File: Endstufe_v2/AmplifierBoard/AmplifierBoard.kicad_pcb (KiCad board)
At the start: 2 copper layers, 125 x 90 mm, 116 parts, among them J1 Conn_01x01_Pin, J10 Conn_02x06_Top_Bottom, J11 B6B-XH-2(LF)(SN), J12 B6B-XH-2(LF)(SN), J13 Conn_01x02_Pin, J14 Conn_01x02_Pin, J15 Conn_01x02_Pin, J16 Conn_01x04, J17 Conn_01x02_Pin, J2 Conn_01x01_Pin, J3 banana connector, J4 banana connector, J5 banana connector, J6 banana connector, J7 banana connector, J8 banana connector, J9 ST-0322D00-071-1A2H, U1 TPA3126D2DADR, U2 TPA3126D2DADR, U3 NVTFWS014P04M8LTAG, U4 1SMA5927A

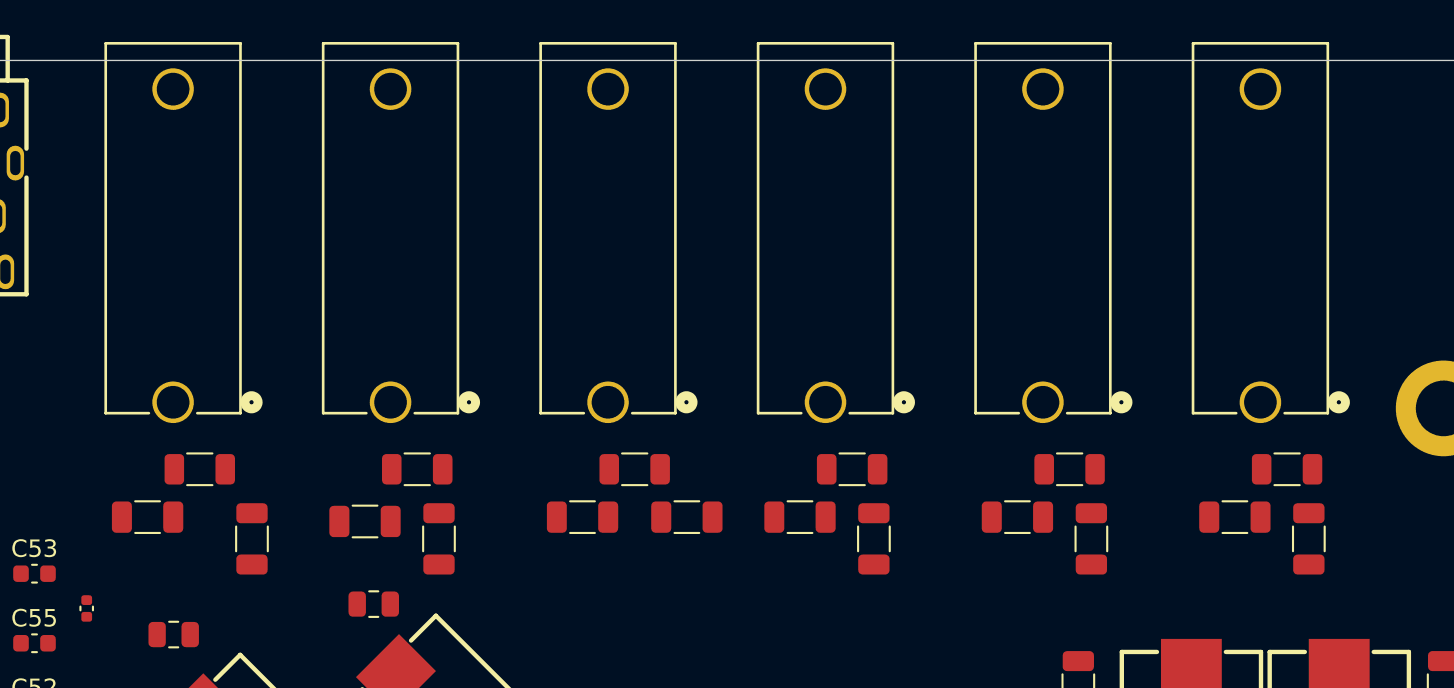
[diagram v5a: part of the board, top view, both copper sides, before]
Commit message: Finalize layout and check DRC
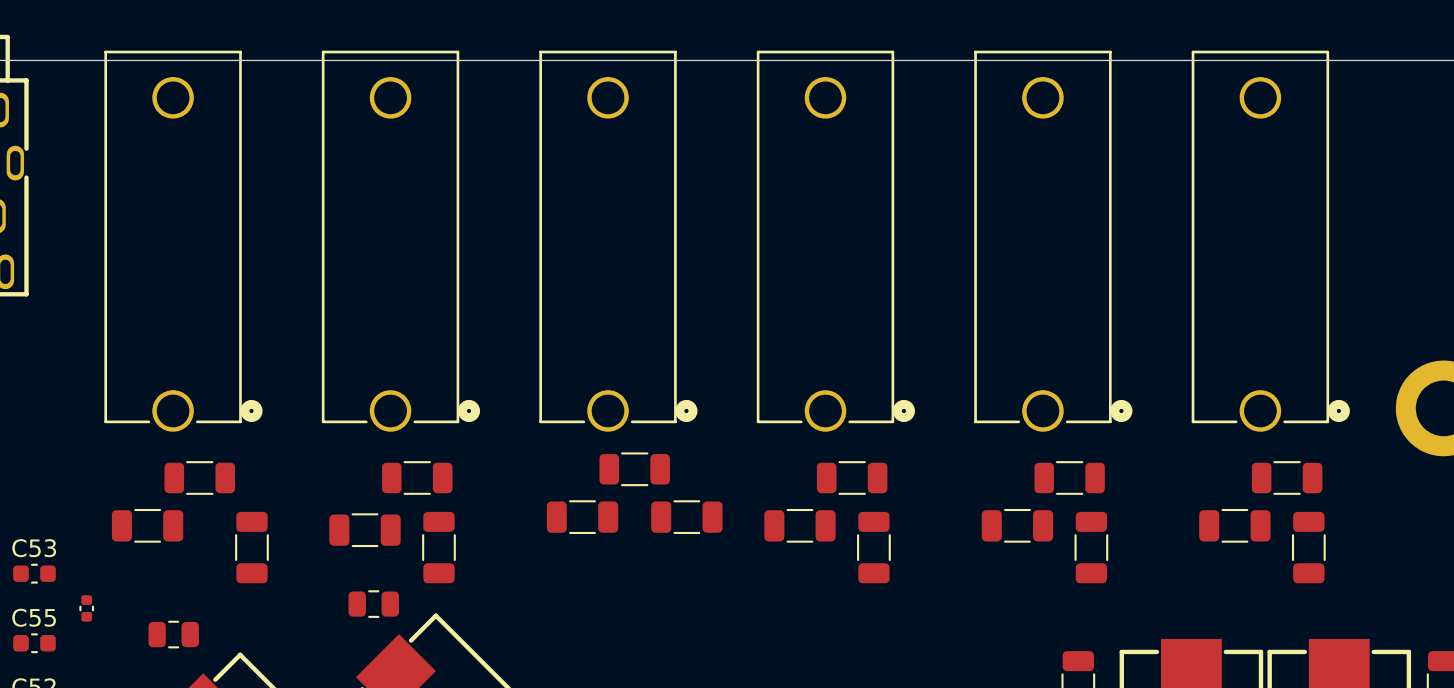
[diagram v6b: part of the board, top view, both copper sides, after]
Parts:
- moved C41 0.50 mm to (193.0, 76.8)
- moved C42 0.50 mm to (205.5, 76.8)
- moved C43 0.50 mm to (218.0, 76.8)
- moved C44 0.50 mm to (155.5, 76.8)
- moved C45 0.50 mm to (168.0, 77.0)
- moved C47 0.50 mm to (197.2, 78.0)
- moved C48 0.50 mm to (209.8, 78.0)
- moved C49 0.50 mm to (222.2, 78.0)
- moved C50 0.50 mm to (161.5, 78.0)
- moved C51 0.50 mm to (172.2, 78.0)
- moved J3 0.50 mm to (182.0, 70.1)
- moved J4 0.50 mm to (194.5, 70.1)
- moved J5 0.50 mm to (207.0, 70.1)
- moved J6 0.50 mm to (219.5, 70.1)
- moved J7 0.50 mm to (157.0, 70.1)
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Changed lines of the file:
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@@
 	(footprint "Endstufe:R_1206_3216Metric"
 		(layer "F.Cu")
-		(at 221 73.5 180)
+		(at 221 74 180)
 		(descr "Resistor SMD 1206 (3216 Metric), square (rectangular) end terminal, IPC_7351 nominal, (Body size source: IPC-SM-782 page 72, https://www.pcb-3d.com/wordpress/wp-content/uploads/ipc-sm-782a_amendment_1_and_2.pdf), generated with kicad-footprint-generator")
 		(tags "resistor")
@@
 	(footprint "Endstufe:C_1206_3216Metric"
 		(layer "F.Cu")
-		(at 155.5 76.25 180)
+		(at 155.5 76.75 180)
 		(descr "Capacitor SMD 1206 (3216 Metric), square (rectangular) end terminal, IPC_7351 nominal, (Body size source: IPC-SM-782 page 76, https://www.pcb-3d.com/wordpress/wp-content/uploads/ipc-sm-782a_amendment_1_and_2.pdf), generated with kicad-footprint-generator")
 		(tags "capacitor")
@@
 	(footprint "Endstufe:C_1206_3216Metric"
 		(layer "F.Cu")
-		(at 172.25 77.5 90)
+		(at 172.25 78 90)
 		(descr "Capacitor SMD 1206 (3216 Metric), square (rectangular) end terminal, IPC_7351 nominal, (Body size source: IPC-SM-782 page 76, https://www.pcb-3d.com/wordpress/wp-content/uploads/ipc-sm-782a_amendment_1_and_2.pdf), generated with kicad-footprint-generator")
 		(tags "capacitor")
@@
 		(tags "capacitor")
 		(property "Reference" "C52"
-			(at 0 -1.43 360)
+			(at 0 -1.43 0)
 			(layer "F.SilkS")
 			(effects
@@
 		)
 		(property "Value" "180nF"
-			(at 0 1.43 360)
+			(at 0 1.43 0)
 			(layer "F.Fab")
 			(effects
@@
 		)
 		(fp_text user "${REFERENCE}"
-			(at 0 0 360)
+			(at 0 0 0)
 			(layer "F.Fab")
 			(effects
@@
 	(footprint "Endstufe:CONN_973582100_HRS"
 		(layer "F.Cu")
-		(at 206.9666 69.648001 180)
+		(at 206.9666 70.148001 180)
 		(tags "973582100 ")
 		(property "Reference" "J5"
@@
 	(footprint "Endstufe:R_1206_3216Metric"
 		(layer "F.Cu")
-		(at 196 73.5 180)
+		(at 196 74 180)
 		(descr "Resistor SMD 1206 (3216 Metric), square (rectangular) end terminal, IPC_7351 nominal, (Body size source: IPC-SM-782 page 72, https://www.pcb-3d.com/wordpress/wp-content/uploads/ipc-sm-782a_amendment_1_and_2.pdf), generated with kicad-footprint-generator")
 		(tags "resistor")
@@
 	(footprint "Endstufe:CONN_973582100_HRS"
 		(layer "F.Cu")
-		(at 156.9666 69.648001 180)
+		(at 156.9666 70.148001 180)
 		(tags "973582100 ")
 		(property "Reference" "J7"
@@
 	(footprint "Endstufe:C_1206_3216Metric"
 		(layer "F.Cu")
-		(at 161.5 77.5 -90)
+		(at 161.5 78 -90)
 		(descr "Capacitor SMD 1206 (3216 Metric), square (rectangular) end terminal, IPC_7351 nominal, (Body size source: IPC-SM-782 page 76, https://www.pcb-3d.com/wordpress/wp-content/uploads/ipc-sm-782a_amendment_1_and_2.pdf), generated with kicad-footprint-generator")
 		(tags "capacitor")
@@
 		(tags "capacitor")
 		(property "Reference" "C55"
-			(at 0 -1.43 360)
+			(at 0 -1.43 0)
 			(layer "F.SilkS")
 			(effects
@@
 		)
 		(property "Value" "180nF"
-			(at 0 1.43 360)
+			(at 0 1.43 0)
 			(layer "F.Fab")
 			(effects
@@
 		)
 		(fp_text user "${REFERENCE}"
-			(at 0 0 360)
+			(at 0 0 0)
 			(layer "F.Fab")
 			(effects
@@
 	(footprint "Endstufe:C_1206_3216Metric"
 		(layer "F.Cu")
-		(at 168 76.5)
+		(at 168 77)
 		(descr "Capacitor SMD 1206 (3216 Metric), square (rectangular) end terminal, IPC_7351 nominal, (Body size source: IPC-SM-782 page 76, https://www.pcb-3d.com/wordpress/wp-content/uploads/ipc-sm-782a_amendment_1_and_2.pdf), generated with kicad-footprint-generator")
 		(tags "capacitor")
@@
 	(footprint "Endstufe:R_1206_3216Metric"
 		(layer "F.Cu")
-		(at 171 73.5 180)
+		(at 171 74 180)
 		(descr "Resistor SMD 1206 (3216 Metric), square (rectangular) end terminal, IPC_7351 nominal, (Body size source: IPC-SM-782 page 72, https://www.pcb-3d.com/wordpress/wp-content/uploads/ipc-sm-782a_amendment_1_and_2.pdf), generated with kicad-footprint-generator")
 		(tags "resistor")
@@
 	(footprint "Endstufe:C_1206_3216Metric"
 		(layer "F.Cu")
-		(at 222.25 77.5 90)
+		(at 222.25 78 90)
 		(descr "Capacitor SMD 1206 (3216 Metric), square (rectangular) end terminal, IPC_7351 nominal, (Body size source: IPC-SM-782 page 76, https://www.pcb-3d.com/wordpress/wp-content/uploads/ipc-sm-782a_amendment_1_and_2.pdf), generated with kicad-footprint-generator")
 		(tags "capacitor")
@@
 	(footprint "Endstufe:R_1206_3216Metric"
 		(layer "F.Cu")
-		(at 158.5 73.5)
+		(at 158.5 74)
 		(descr "Resistor SMD 1206 (3216 Metric), square (rectangular) end terminal, IPC_7351 nominal, (Body size source: IPC-SM-782 page 72, https://www.pcb-3d.com/wordpress/wp-content/uploads/ipc-sm-782a_amendment_1_and_2.pdf), generated with kicad-footprint-generator")
 		(tags "resistor")
@@
 	(footprint "Endstufe:CONN_973582100_HRS"
 		(layer "F.Cu")
-		(at 194.4666 69.648001 180)
+		(at 194.4666 70.148001 180)
 		(tags "973582100 ")
 		(property "Reference" "J4"
@@
 	(footprint "Endstufe:CONN_973582100_HRS"
 		(layer "F.Cu")
-		(at 181.9666 69.648001 180)
+		(at 181.9666 70.148001 180)
 		(tags "973582100 ")
 		(property "Reference" "J3"
@@
 		(tags "Through hole pin header THT 2x06 2.54mm double row")
 		(property "Reference" "J10"
-			(at 1.27 -2.33 360)
+			(at 1.27 -2.33 0)
 			(layer "F.SilkS")
 			(effects
@@
 		)
 		(property "Value" "Conn_02x06_Top_Bottom"
-			(at 1.27 15.03 360)
+			(at 1.27 15.03 0)
 			(layer "F.Fab")
 			(effects
@@
 		(tags "capacitor")
 		(property "Reference" "C54"
-			(at 0 -1.43 360)
+			(at 0 -1.43 0)
 			(layer "F.SilkS")
 			(effects
@@
 		)
 		(property "Value" "180nF"
-			(at 0 1.43 360)
+			(at 0 1.43 0)
 			(layer "F.Fab")
 			(effects
@@
 		)
 		(fp_text user "${REFERENCE}"
-			(at 0 0 360)
+			(at 0 0 0)
 			(layer "F.Fab")
 			(effects
@@
 	(footprint "Endstufe:C_1206_3216Metric"
 		(layer "F.Cu")
-		(at 218 76.25)
+		(at 218 76.75)
 		(descr "Capacitor SMD 1206 (3216 Metric), square (rectangular) end terminal, IPC_7351 nominal, (Body size source: IPC-SM-782 page 76, https://www.pcb-3d.com/wordpress/wp-content/uploads/ipc-sm-782a_amendment_1_and_2.pdf), generated with kicad-footprint-generator")
 		(tags "capacitor")
@@
 	(footprint "Endstufe:R_1206_3216Metric"
 		(layer "F.Cu")
-		(at 208.5 73.5)
+		(at 208.5 74)
 		(descr "Resistor SMD 1206 (3216 Metric), square (rectangular) end terminal, IPC_7351 nominal, (Body size source: IPC-SM-782 page 72, https://www.pcb-3d.com/wordpress/wp-content/uploads/ipc-sm-782a_amendment_1_and_2.pdf), generated with kicad-footprint-generator")
 		(tags "resistor")
@@
 	(footprint "Endstufe:C_1206_3216Metric"
 		(layer "F.Cu")
-		(at 209.75 77.5 -90)
+		(at 209.75 78 -90)
 		(descr "Capacitor SMD 1206 (3216 Metric), square (rectangular) end terminal, IPC_7351 nominal, (Body size source: IPC-SM-782 page 76, https://www.pcb-3d.com/wordpress/wp-content/uploads/ipc-sm-782a_amendment_1_and_2.pdf), generated with kicad-footprint-generator")
 		(tags "capacitor")
@@
 	(footprint "Endstufe:C_1206_3216Metric"
 		(layer "F.Cu")
-		(at 205.5 76.25 180)
+		(at 205.5 76.75 180)
 		(descr "Capacitor SMD 1206 (3216 Metric), square (rectangular) end terminal, IPC_7351 nominal, (Body size source: IPC-SM-782 page 76, https://www.pcb-3d.com/wordpress/wp-content/uploads/ipc-sm-782a_amendment_1_and_2.pdf), generated with kicad-footprint-generator")
 		(tags "capacitor")
@@
 	(footprint "Endstufe:CONN_973582100_HRS"
 		(layer "F.Cu")
-		(at 169.4666 69.648001 180)
+		(at 169.4666 70.148001 180)
 		(tags "973582100 ")
 		(property "Reference" "J8"
@@
 	(footprint "Endstufe:C_1206_3216Metric"
 		(layer "F.Cu")
-		(at 197.25 77.5 90)
+		(at 197.25 78 90)
 		(descr "Capacitor SMD 1206 (3216 Metric), square (rectangular) end terminal, IPC_7351 nominal, (Body size source: IPC-SM-782 page 76, https://www.pcb-3d.com/wordpress/wp-content/uploads/ipc-sm-782a_amendment_1_and_2.pdf), generated with kicad-footprint-generator")
 		(tags "capacitor")
@@
 		(tags "capacitor")
 		(property "Reference" "C53"
-			(at 0 -1.43 360)
+			(at 0 -1.43 0)
 			(layer "F.SilkS")
 			(effects
@@
 		)
 		(property "Value" "180nF"
-			(at 0 1.43 360)
+			(at 0 1.43 0)
 			(layer "F.Fab")
 			(effects
@@
 		)
 		(fp_text user "${REFERENCE}"
-			(at 0 0 360)
+			(at 0 0 0)
 			(layer "F.Fab")
 			(effects
@@
 	(footprint "Endstufe:CONN_973582100_HRS"
 		(layer "F.Cu")
-		(at 219.4666 69.648001 180)
+		(at 219.4666 70.148001 180)
 		(tags "973582100 ")
 		(property "Reference" "J6"
@@
 	(footprint "Endstufe:C_1206_3216Metric"
 		(layer "F.Cu")
-		(at 193 76.25)
+		(at 193 76.75)
 		(descr "Capacitor SMD 1206 (3216 Metric), square (rectangular) end terminal, IPC_7351 nominal, (Body size source: IPC-SM-782 page 76, https://www.pcb-3d.com/wordpress/wp-content/uploads/ipc-sm-782a_amendment_1_and_2.pdf), generated with kicad-footprint-generator")
 		(tags "capacitor")

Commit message: Select some design rules for PCB layouting
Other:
- copper layers 2 -> 4
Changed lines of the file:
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@@
 	(generator_version "8.0")
 	(general
-		(thickness 1.6)
+		(thickness 1.5842)
 		(legacy_teardrops no)
 	)
@@
 	(layers
 		(0 "F.Cu" signal)
+		(1 "In1.Cu" signal)
+		(2 "In2.Cu" signal)
 		(31 "B.Cu" signal)
 		(32 "B.Adhes" user "B.Adhesive")
@@
 	)
 	(setup
+		(stackup
+			(layer "F.SilkS"
+				(type "Top Silk Screen")
+			)
+			(layer "F.Paste"
+				(type "Top Solder Paste")
+			)
+			(layer "F.Mask"
+				(type "Top Solder Mask")
+				(thickness 0.01)
+			)
+			(layer "F.Cu"
+				(type "copper")
+				(thickness 0.035)
+			)
+			(layer "dielectric 1"
+				(type "prepreg")
+				(color "FR4 natural")
+				(thickness 0.0994)
+				(material "3313")
+				(epsilon_r 4.1)
+				(loss_tangent 0.02)
+			)
+			(layer "In1.Cu"
+				(type "copper")
+				(thickness 0.0152)
+			)
+			(layer "dielectric 2"
+				(type "core")
+				(color "FR4 natural")
+				(thickness 1.265)
+				(material "JLCPCB Core")
+				(epsilon_r 4.6)
+				(loss_tangent 0.02)
+			)
+			(layer "In2.Cu"
+				(type "copper")
+				(thickness 0.0152)
+			)
+			(layer "dielectric 3"
+				(type "prepreg")
+				(color "FR4 natural")
+				(thickness 0.0994)
+				(material "3313")
+				(epsilon_r 4.1)
+				(loss_tangent 0.02)
+			)
+			(layer "B.Cu"
+				(type "copper")
+				(thickness 0.035)
+			)
+			(layer "B.Mask"
+				(type "Bottom Solder Mask")
+				(thickness 0.01)
+			)
+			(layer "B.Paste"
+				(type "Bottom Solder Paste")
+			)
+			(layer "B.SilkS"
+				(type "Bottom Silk Screen")
+			)
+			(copper_finish "None")
+			(dielectric_constraints yes)
+		)
 		(pad_to_mask_clearance 0)
 		(allow_soldermask_bridges_in_footprints no)

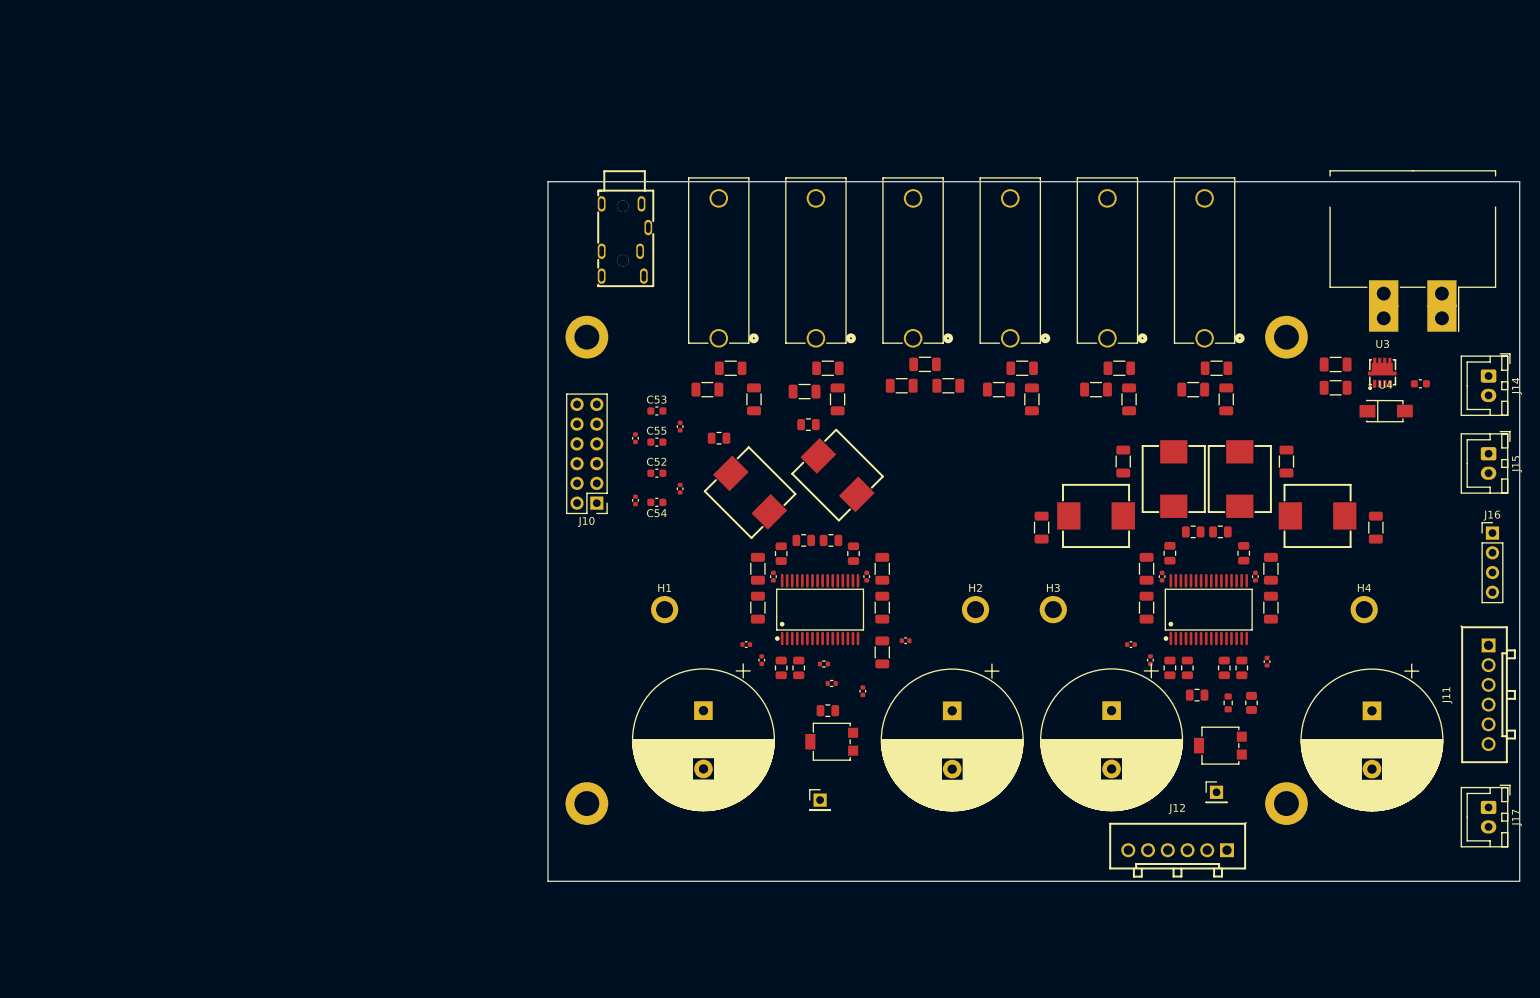
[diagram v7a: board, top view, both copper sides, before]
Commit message: Add resistor divider so 24V pull up can be connected to RP2040
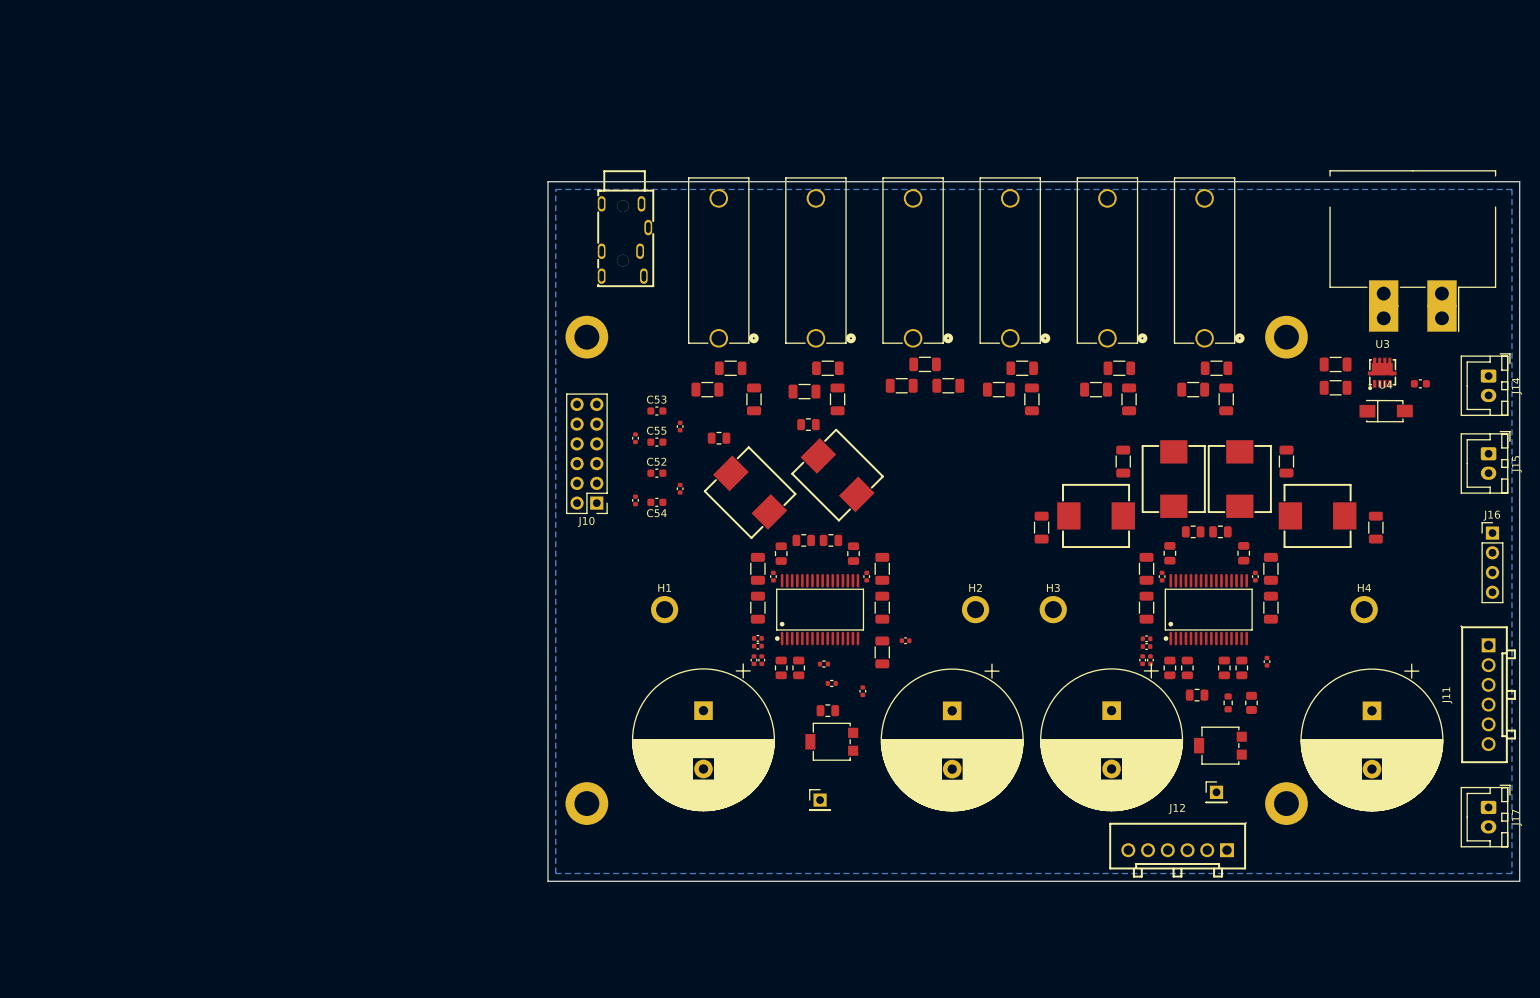
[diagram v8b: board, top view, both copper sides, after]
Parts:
- added R23: 1k5, Endstufe:C_0402_1005Metric, F.Cu at (211.5, 111.5)
- added R24: 1k5, Endstufe:C_0402_1005Metric, F.Cu at (212.0, 108.8)
- added R25: 1k5, Endstufe:C_0402_1005Metric, F.Cu at (162.0, 108.8)
- added R26: 1k5, Endstufe:C_0402_1005Metric, F.Cu at (161.5, 111.5)
- moved R6 2.02 mm to (212.0, 109.8)
- moved R7 1.51 mm to (162.0, 109.8)
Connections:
- R6 pad 2: +3V3 -> +24V
- R7 pad 2: +3V3 -> +24V
- R8 pad 2: +3V3 -> +24V
- R9 pad 2: +3V3 -> +24V
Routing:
- added copper zone on B.Cu, net +24V
- added copper zone on In1.Cu, net GND
- added copper zone on In2.Cu, net GND
